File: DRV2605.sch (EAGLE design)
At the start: 0 parts

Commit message: board placement for first DRV
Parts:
- added C1, C11, C13, C2, C4, C6, C8: 1.0uF, SparkFun-Capacitors:1.0UF-16V-10%(0402)
- added C10, C12, C14, C3, C5, C7, C9: 1.0uF, rcl:C-USC0402
- added I2C1, I2C10, I2C11, I2C12, I2C13, I2C14, I2C2, I2C3, I2C4, I2C5, I2C6, I2C7, I2C8, I2C9: JUMPER-PAD-3-NC_BY_PASTE, SparkFun-Passives:JUMPER-PAD-3-NC_BY_PASTE
- added R1, R10, R11, R12, R13, R14, R2, R3, R4, R5, R6, R7, R8, R9: 2.2k, SparkFun-Resistors:2.2KOHM-1/10W-1%(0603)
- added U1, U2, U3, U4, U5, U6, U7: DRV2605L, SparkFun-PowerIC:DRV2605L
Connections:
- new net +OUT1: U2.OUT+
- new net +OUT2: U3.OUT+
- new net +OUT3: U4.OUT+
- new net +OUT4: U5.OUT+
- new net +OUT5: U1.OUT+
- new net +OUT6: U6.OUT+
- new net +OUT7: U7.OUT+
- new net -OUT1: U2.OUT-
- new net -OUT2: U3.OUT-
- new net -OUT3: U4.OUT-
- new net -OUT4: U5.OUT-
- new net -OUT5: U1.OUT-
- new net -OUT6: U6.OUT-
- new net -OUT7: U7.OUT-
- new net COMMON_EN: I2C10.3, I2C12.3, I2C14.3, I2C2.3, I2C4.3, I2C6.3, I2C8.3
- new net EN1: I2C2.2, U2.EN
- new net EN2: I2C4.2, U3.EN
- new net EN3: I2C6.2, U4.EN
- new net EN4: I2C8.2, U5.EN
- new net EN5: I2C10.2, U1.EN
- new net EN6: I2C12.2, U6.EN
- new net EN7: I2C14.2, U7.EN
- new net GND: C1.2, C10.2, C11.2, C12.2, C13.2, C14.2, C2.2, C3.2, C4.2, C5.2, C6.2, C7.2, C8.2, C9.2, U1.GND, U2.GND, U3.GND, U4.GND, U5.GND, U6.GND, U7.GND
- new net IN/TRIG1: U2.IN/TRIG
- new net IN/TRIG2: U3.IN/TRIG
- new net IN/TRIG3: U4.IN/TRIG
- new net IN/TRIG4: U5.IN/TRIG
- new net IN/TRIG5: U1.IN/TRIG
- new net IN/TRIG6: U6.IN/TRIG
- new net IN/TRIG7: U7.IN/TRIG
- new net N$1: C3.1, U1.REG
- new net N$10: C9.1, U2.REG
- new net N$11: I2C1.3, R4.2
- new net N$12: I2C1.1, R3.2
- new net N$13: C5.1, U3.REG
- new net N$14: I2C3.3, R6.2
- new net N$15: I2C3.1, R5.2
- new net N$16: C7.1, U4.REG
- new net N$17: I2C5.3, R8.2
- new net N$18: I2C5.1, R7.2
- new net N$19: C10.1, U5.REG
- new net N$2: I2C9.3, R2.2
- new net N$20: I2C7.3, R10.2
- new net N$21: I2C7.1, R9.2
- new net N$3: I2C9.1, R1.2
- new net N$4: C12.1, U6.REG
- new net N$5: I2C11.3, R12.2
- new net N$6: I2C11.1, R11.2
- new net N$7: C14.1, U7.REG
- new net N$8: I2C13.3, R14.2
- new net N$9: I2C13.1, R13.2
- new net SCL1: R3.1, U2.SCL
- new net SCL2: R5.1, U3.SCL
- new net SCL3: R7.1, U4.SCL
- new net SCL4: R9.1, U5.SCL
- new net SCL5: R1.1, U1.SCL
- new net SCL6: R11.1, U6.SCL
- new net SCL7: R13.1, U7.SCL
- new net SDA1: R4.1, U2.SDA
- new net SDA2: R6.1, U3.SDA
- new net SDA3: R8.1, U4.SDA
- new net SDA4: R10.1, U5.SDA
- new net SDA5: R2.1, U1.SDA
- new net SDA6: R12.1, U6.SDA
- new net SDA7: R14.1, U7.SDA
- new net VCC: C1.1, C11.1, C13.1, C2.1, C4.1, C6.1, C8.1, I2C1.2, I2C10.1, I2C11.2, I2C12.1, I2C13.2, I2C14.1, I2C2.1, I2C3.2, I2C4.1, I2C5.2, I2C6.1, I2C7.2, I2C8.1, I2C9.2, U1.VDD, U1.VDD/NC, U2.VDD, U2.VDD/NC, U3.VDD, U3.VDD/NC, U4.VDD, U4.VDD/NC, U5.VDD, U5.VDD/NC, U6.VDD, U6.VDD/NC, U7.VDD, U7.VDD/NC
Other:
- note added: "Clear jumper to remove pull-ups from I2C bus"

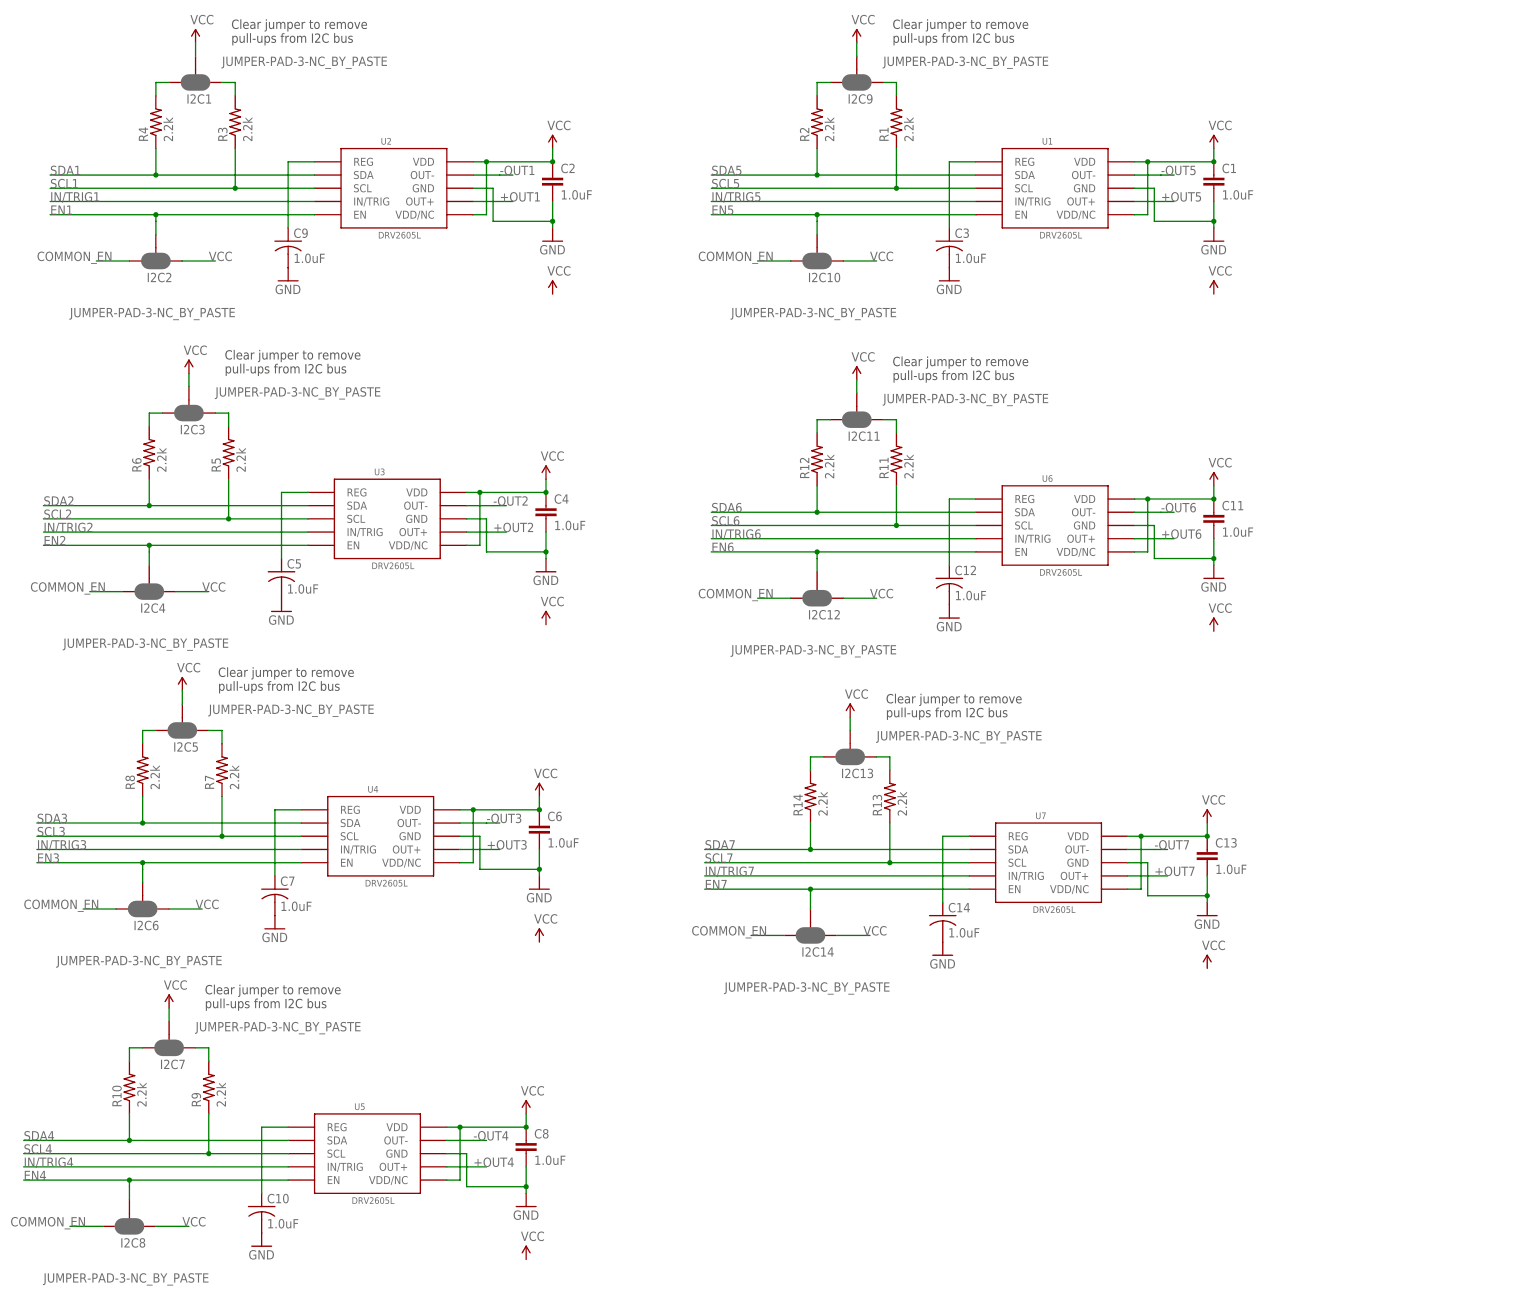
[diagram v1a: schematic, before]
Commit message: DRV routing done
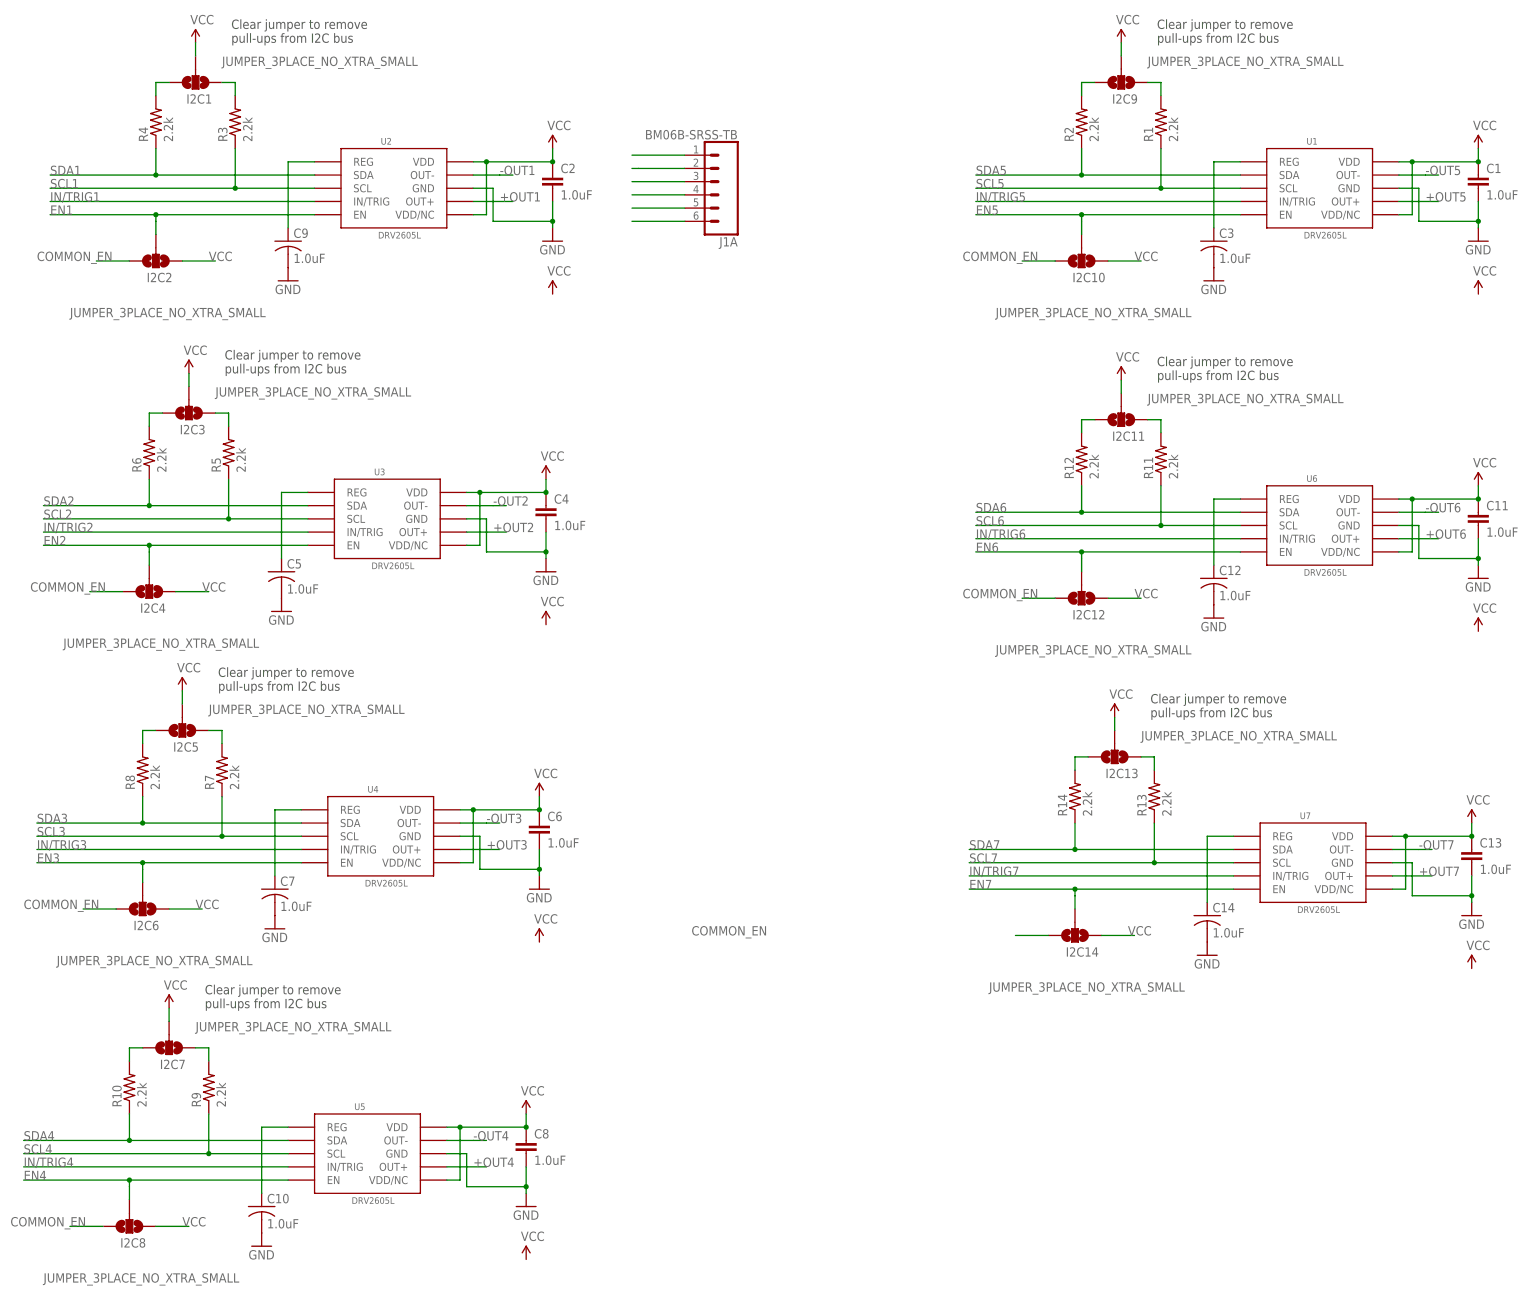
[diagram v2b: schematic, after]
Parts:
- added J1: BM06B-SRSS-TB, SparkFun-Connectors:JST_6_PIN_HORIZONTAL
- I2C1, I2C10, I2C11, I2C12, I2C13, I2C14, I2C2, I2C3, I2C4, I2C5, I2C6, I2C7, I2C8, I2C9: value JUMPER-PAD-3-NC_BY_PASTE -> JUMPER_3PLACE_NO_XTRA_SMALL; device SparkFun-Passives:JUMPER-PAD-3-NC_BY_PASTE -> yhtomit_jumpers:JUMPER_3PLACE_NO_XTRA_SMALL
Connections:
- new net N$22: J1A.1
- new net N$23: J1A.2
- new net N$24: J1A.3
- new net N$25: J1A.4
- new net N$26: J1A.5
- new net N$27: J1A.6
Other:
- moved on the sheet: C1, C11, C12, C13, C14, C3, R1, R11, R12, R13, R14, R2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

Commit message: TCA added and routed to 5 fingers
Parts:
- added C15, C16: 10uF, resistor:C-USC0402
- added J2, J3, J4, J5: BM06B-SRSS-TB, SparkFun-Connectors:JST_6_PIN_HORIZONTAL
- added J7: (no value), SparkFun-Connectors:CONN_04SMD2
- added R15, R16, R17, R18, R19, R20: 10K, rcl:R-US_R0402
- added SCLPU, SCLPU1, SDAPU, SDAPU1: JUMPER_2PLACE_NO_XTRA_SMALL, yhtomit_jumpers:JUMPER_2PLACE_NO_XTRA_SMALL
- added U$5, U$6: JUMPER_3PLACE_NO_XTRA_SMALL, yhtomit_jumpers:JUMPER_3PLACE_NO_XTRA_SMALL
- added U8, U9: TCA9548APWR, microbuilder:TCA9548A
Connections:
- new net 0SCL: U8.SCL0
- new net 0SCL1: U9.SCL0
- new net 0SDA: U8.SDA0
- new net 0SDA1: U9.SDA0
- new net 1SCL: U8.SCL1
- new net 1SCL1: U9.SCL1
- new net 1SDA: U8.SDA1
- new net 1SDA1: U9.SDA1
- new net 2SCL: U8.SCL2
- new net 2SCL1: U9.SCL2
- new net 2SDA: U8.SDA2
- new net 2SDA1: U9.SDA2
- new net 3SCL1: U9.SCL3
- new net 3SDA1: U9.SDA3
- new net 4SCL1: U9.SCL4
- new net 4SDA1: U9.SDA4
- new net 5SCL1: U9.SCL5
- new net 5SDA1: U9.SDA5
- new net 6SCL1: U9.SCL6
- new net 6SDA1: U9.SDA6
- new net 7SCL1: U9.SCL7
- new net 7SDA1: U9.SDA7
- new net INPUTSCL: SCLPU.1, U8.SCL
- new net INPUTSCL1: SCLPU1.1, U9.SCL
- new net INPUTSDA: SDAPU.1, U8.SDA
- new net INPUTSDA1: SDAPU1.1, U9.SDA
- new net N$28: J2A.4
- new net N$29: J2A.5
- new net N$30: U$6.2, U8.A1
- new net N$32: J3A.4
- new net N$33: J3A.5
- new net N$36: J4A.4
- new net N$37: J4A.5
- new net N$40: J5A.4
- new net N$41: J5A.5
- new net N$42: R19.1, SCLPU1.2
- new net N$43: R18.1, SDAPU1.2
- new net RESET: R17.1, U8.#RESET
- new net RESET1: R20.1, U9.#RESET
- net +OUT1: now also J1A.3
- net +OUT2: now also J2A.3
- net +OUT3: now also J3A.3
- net +OUT4: now also J4A.3
- net +OUT5: now also J5A.3
- net +OUT6: now also J7.3
- net +OUT7: now also J7.1
- net -OUT1: now also J1A.2
- net -OUT2: now also J2A.2
- net -OUT3: now also J3A.2
- net -OUT4: now also J4A.2
- net -OUT5: now also J5A.2
- net -OUT6: now also J7.4
- net -OUT7: now also J7.2
- net GND: now also C15.2, C16.2, J1A.1, J2A.1, J3A.1, J4A.1, J5A.1, U$5.1, U$6.1, U8.GND, U9.A0, U9.A1, U9.A2, U9.GND
- net N$22: now also U8.A2; no longer J1A.1
- net N$23: now also R16.1, SCLPU.2; no longer J1A.2
- net N$24: now also R15.1, SDAPU.2; no longer J1A.3
- net N$27: now also U$5.2, U8.A0; no longer J1A.6
- net SCL1: now also U8.SCL7
- net SCL2: now also U8.SCL6
- net SCL3: now also U8.SCL5
- net SCL4: now also U8.SCL4
- net SCL5: now also U8.SCL3
- net SDA1: now also U8.SDA7
- net SDA2: now also U8.SDA6
- net SDA3: now also U8.SDA5
- net SDA4: now also U8.SDA4
- net SDA5: now also U8.SDA3
- net VCC: now also C15.1, C16.1, J1A.6, J2A.6, J3A.6, J4A.6, J5A.6, R15.2, R16.2, R17.2, R18.2, R19.2, R20.2, U$5.3, U$6.3, U8.VCC, U9.VCC

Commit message: working on control pins
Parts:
- removed I2C1, I2C11, I2C13, I2C3, I2C5, I2C7, I2C9: JUMPER_3PLACE_NO_XTRA_SMALL, yhtomit_jumpers:JUMPER_3PLACE_NO_XTRA_SMALL
- removed SCLPU, SCLPU1, SDAPU, SDAPU1: JUMPER_2PLACE_NO_XTRA_SMALL, yhtomit_jumpers:JUMPER_2PLACE_NO_XTRA_SMALL
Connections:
- net 2SCL1 renamed IMU_SCL6
- net 2SDA1 renamed IMU_SDA6
- removed net 3SCL1: U9.SCL3
- removed net 3SDA1: U9.SDA3
- removed net 4SCL1: U9.SCL4
- removed net 4SDA1: U9.SDA4
- removed net 5SCL1: U9.SCL5
- removed net 5SDA1: U9.SDA5
- removed net 6SCL1: U9.SCL6
- removed net 6SDA1: U9.SDA6
- removed net 7SCL1: U9.SCL7
- removed net 7SDA1: U9.SDA7
- removed net N$11: I2C1.3, R4.2
- removed net N$12: I2C1.1, R3.2
- removed net N$14: I2C3.3, R6.2
- removed net N$15: I2C3.1, R5.2
- removed net N$17: I2C5.3, R8.2
- removed net N$18: I2C5.1, R7.2
- removed net N$2: I2C9.3, R2.2
- removed net N$20: I2C7.3, R10.2
- removed net N$21: I2C7.1, R9.2
- removed net N$23: R16.1, SCLPU.2
- removed net N$24: R15.1, SDAPU.2
- removed net N$25: J1A.4
- removed net N$26: J1A.5
- removed net N$28: J2A.4
- removed net N$29: J2A.5
- removed net N$3: I2C9.1, R1.2
- removed net N$32: J3A.4
- removed net N$33: J3A.5
- removed net N$36: J4A.4
- removed net N$37: J4A.5
- removed net N$40: J5A.4
- removed net N$41: J5A.5
- removed net N$42: R19.1, SCLPU1.2
- removed net N$43: R18.1, SDAPU1.2
- removed net N$5: I2C11.3, R12.2
- removed net N$6: I2C11.1, R11.2
- removed net N$8: I2C13.3, R14.2
- removed net N$9: I2C13.1, R13.2
- new net IMU_SCL1: J1A.5, U9.SCL7
- new net IMU_SCL2: J2A.5, U9.SCL6
- new net IMU_SCL3: J3A.5, U9.SCL5
- new net IMU_SCL4: J4A.5, U9.SCL4
- new net IMU_SCL5: J5A.5, U9.SCL3
- new net IMU_SDA1: J1A.4, U9.SDA7
- new net IMU_SDA2: J2A.4, U9.SDA6
- new net IMU_SDA3: J3A.4, U9.SDA5
- new net IMU_SDA4: J4A.4, U9.SDA4
- new net IMU_SDA5: J5A.4, U9.SDA3
- net INPUTSCL: now also R16.1; no longer SCLPU.1
- net INPUTSCL1: now also R19.1; no longer SCLPU1.1
- net INPUTSDA: now also R15.1; no longer SDAPU.1
- net INPUTSDA1: now also R18.1; no longer SDAPU1.1
- net VCC: now also R1.2, R10.2, R11.2, R12.2, R13.2, R14.2, R2.2, R3.2, R4.2, R5.2, R6.2, R7.2, R8.2, R9.2; no longer I2C1.2, I2C11.2, I2C13.2, I2C3.2, I2C5.2, I2C7.2, I2C9.2

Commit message: NRF done STM in progress
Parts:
- added C17, C18, C46, C47, C55, C56: 12pF, Nordic_nRF:CAPACITOR_0402_N
- added C19, C20: 22pF, Nordic_nRF:CAPACITOR_0402_N
- added C21: 0.1uf, rcl:C-USC0402
- added C22: 10uf, rcl:C-USC0402
- added C23, C24: 2.2uf, rcl:C-USC0402
- added C48: 2.2nF, Nordic_nRF:CAPACITOR_0402_N
- added C49, C52: 100nF, Nordic_nRF:CAPACITOR_0402_N
- added C50: 47nF, Nordic_nRF:CAPACITOR_0402_N
- added C51: 1.0nF, Nordic_nRF:CAPACITOR_0402_N
- added C53: 4.7µF, Nordic_nRF:CAPACITOR_0603_N
- added C54: 1.0µF, Nordic_nRF:CAPACITOR_0603_N
- added C57: 2.2pF, Nordic_nRF:CAPACITOR_0402_N
- added C58: 1.0pF, Nordic_nRF:CAPACITOR_0402_N
- added C59: 1.5pF, Nordic_nRF:CAPACITOR_0402_N
- added L11: 3.3nH, Nordic_nRF:INDUCTOR_0402_N
- added L12: 10µH, Nordic_nRF:INDUCTOR_0603_N
- added L13: 15nH, Nordic_nRF:INDUCTOR_0402_N
- added L14: 4.7nH, Nordic_nRF:INDUCTOR_0402_N
- added L15: 10nH, Nordic_nRF:INDUCTOR_0402_N
- added R21, R22, R25: 10k, resistor:R-US_R0402
- added R23: 1M, resistor:R-US_R0402
- added U$9: STM32F405RGT6, SparkFun-IC-Microcontroller:STM32F405RG
- added U11: NRF51X22_QFQF, Nordic_nRF:NRF51X22_QFQF
- added X1, X5: 32.768kHz, Nordic_nRF:XTAL_32KHZ
- added X2: 8MHz, Nordic_nRF:XTAL_32KHZ
- added X4: 16MHz, Nordic_nRF:XTAL_32MHZ
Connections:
- removed net 1SCL: U8.SCL1
- removed net 1SDA: U8.SDA1
- removed net 2SCL: U8.SCL2
- removed net 2SDA: U8.SDA2
- removed net N$22: U8.A2
- new net AVDD: C51.1, C54.1, L13.1, U11.AVDD@35, U11.AVDD@36
- new net BLE_RX: U$9.PA9/UART1_TX, U11.P0.07@11
- new net BLE_TX: U$9.PA10/UART1_RX, U11.P0.06@10
- new net N$2: R25.2, U$9.PB2-BOOT1
- new net N$3: R22.1, U$9.BOOT0
- new net N$33: C46.1, U11.XC2@38, X4.3
- new net N$34: L12.1, L13.2
- new net N$35: L12.2, U11.DCC@02
- new net N$36: C50.1, U11.DEC2@29
- new net N$37: C49.1, U11.DEC1@39
- new net N$38: L14.1, L15.2, U11.ANT1@31
- new net N$39: C48.1, L15.1, U11.VDD_PA@30
- new net N$40: C57.1, L14.2, U11.ANT2@32
- new net N$41: C57.2, C58.1, L11.1
- new net N$5: C23.1, U$9.VCAP1
- new net N$6: C24.1, U$9.VCAP2
- new net P0.00: U11.P0.00@04
- new net P0.01: U11.P0.01@05
- new net P0.02: U11.P0.02@06
- new net P0.03: U11.P0.03@07
- new net P0.04: U11.P0.04@08
- new net P0.05: U11.P0.05@09
- new net P0.08: U11.P0.08@14
- new net P0.09: U11.P0.09@15
- new net P0.10: U11.P0.10@16
- new net P0.11: U11.P0.11@17
- new net P0.12: U11.P0.12@18
- new net P0.13: U11.P0.13@19
- new net P0.14: U11.P0.14@20
- new net P0.17: U11.P0.17@25
- new net P0.19: U11.P0.19@27
- new net P0.20: U11.P0.20@28
- new net P0.21: U11.P0.21@40
- new net P0.22: U11.P0.22@41
- new net P0.23: U11.P0.23@42
- new net P0.24: U11.P0.24@43
- new net P0.25: U11.P0.25@44
- new net P0.26/XL1: C19.2, R23.2, U$9.PH0, X2.1
- new net P0.26/XL2: C17.2, C55.2, U$9.PC14, U11.P0.26@45, X1.1, X5.1
- new net P0.27/XL1: C18.2, C56.2, U$9.PC15, U11.P0.27@46, X1.2, X5.2
- new net P0.27/XL2: C20.2, R23.1, U$9.PH1, X2.2
- new net P0.28: U11.P0.28@47
- new net P0.29: U11.P0.29@48
- new net P0.30: U11.P0.30@03
- new net RF: C59.1, L11.2
- new net RST: R21.2, U$9.NRST
- new net SWDCLK: U11.SWDCLK@24
- new net SWDIO: U11.P0.18@26
- new net SWDIO/NRESET: U11.SWDIO/NRESET@23
- new net VDDA: C21.1, C22.1, R21.1, U$9.VDDA
- new net VDD_NRF: C52.1, C53.1, U11.VDD@01, U11.VDD@12
- new net X2: C47.1, U11.XC1@37, X4.1
- net +OUT1: now also J1A.2; no longer J1A.3
- net +OUT2: now also J2A.2; no longer J2A.3
- net +OUT3: now also J3A.2; no longer J3A.3
- net +OUT4: now also J4A.2; no longer J4A.3
- net +OUT5: now also J5A.2; no longer J5A.3
- net -OUT1: now also J1A.3; no longer J1A.2
- net -OUT2: now also J2A.3; no longer J2A.2
- net -OUT3: now also J3A.3; no longer J3A.2
- net -OUT4: now also J4A.3; no longer J4A.2
- net -OUT5: now also J5A.3; no longer J5A.2
- net GND: now also C17.1, C18.1, C19.1, C20.1, C21.2, C22.2, C23.2, C24.2, C46.2, C47.2, C48.2, C49.2, C50.2, C51.2, C52.2, C53.2, C54.2, C55.1, C56.1, C58.2, C59.2, R22.2, R25.1, U$9.VSSA, U11.VSS@13, U11.VSS@33, U11.VSS@34, U8.A2, X4.2, X4.4
- net INPUTSCL: now also U$9.PB10
- net INPUTSCL1: now also U$9.PB6
- net INPUTSDA: now also U$9.PB11
- net INPUTSDA1: now also U$9.PB7
- net SCL6: now also U8.SCL2
- net SCL7: now also U8.SCL1
- net SDA6: now also U8.SDA2
- net SDA7: now also U8.SDA1
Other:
- note added: "Boot from flash"
- note added: "Boot0 = 0"
- note added: "Boot1 = 0"
- note added: "NRF chip circuit"
- note added: "Optional"
- note added: "TCA Chip Circuit"
- moved on the sheet: C15, C16, R15, R16, R17, R18, R19, R20, U$5, U$6, U8, U9

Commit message: NRF done STM in progress
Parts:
- added C25, C26, C27, C28, C29, C30: 0.1uf, rcl:C-USC0402
- added C31: 10uf, rcl:C-USC0402
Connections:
- removed net VDDA: C21.1, C22.1, R21.1, U$9.VDDA
- net GND: now also C25.2, C26.2, C27.2, C28.2, C29.2, C30.2, C31.2, U$9.VSS1, U$9.VSS2
- net RST: now also C28.1
- net VCC: now also C21.1, C22.1, C25.1, C26.1, C27.1, C29.1, C30.1, C31.1, R21.1, U$9.VBAT, U$9.VDD1, U$9.VDD2, U$9.VDD3, U$9.VDD4, U$9.VDDA
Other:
- moved on the sheet: C21, C22
